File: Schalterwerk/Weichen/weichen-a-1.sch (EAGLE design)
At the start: 44 parts, among them J1 PHNX_2P_508CONN_1017491, Q1 P-MOSFET, Q2 P-MOSFET, Q3 P-MOSFET, Q4 P-MOSFET, X1 PHNX_4P_508CONN_1017493, X2 PHNX_4P_350CONN_1984989_PXC, X3 PHNX_4P_350CONN_1984989_PXC, X4 RJ45-JACK

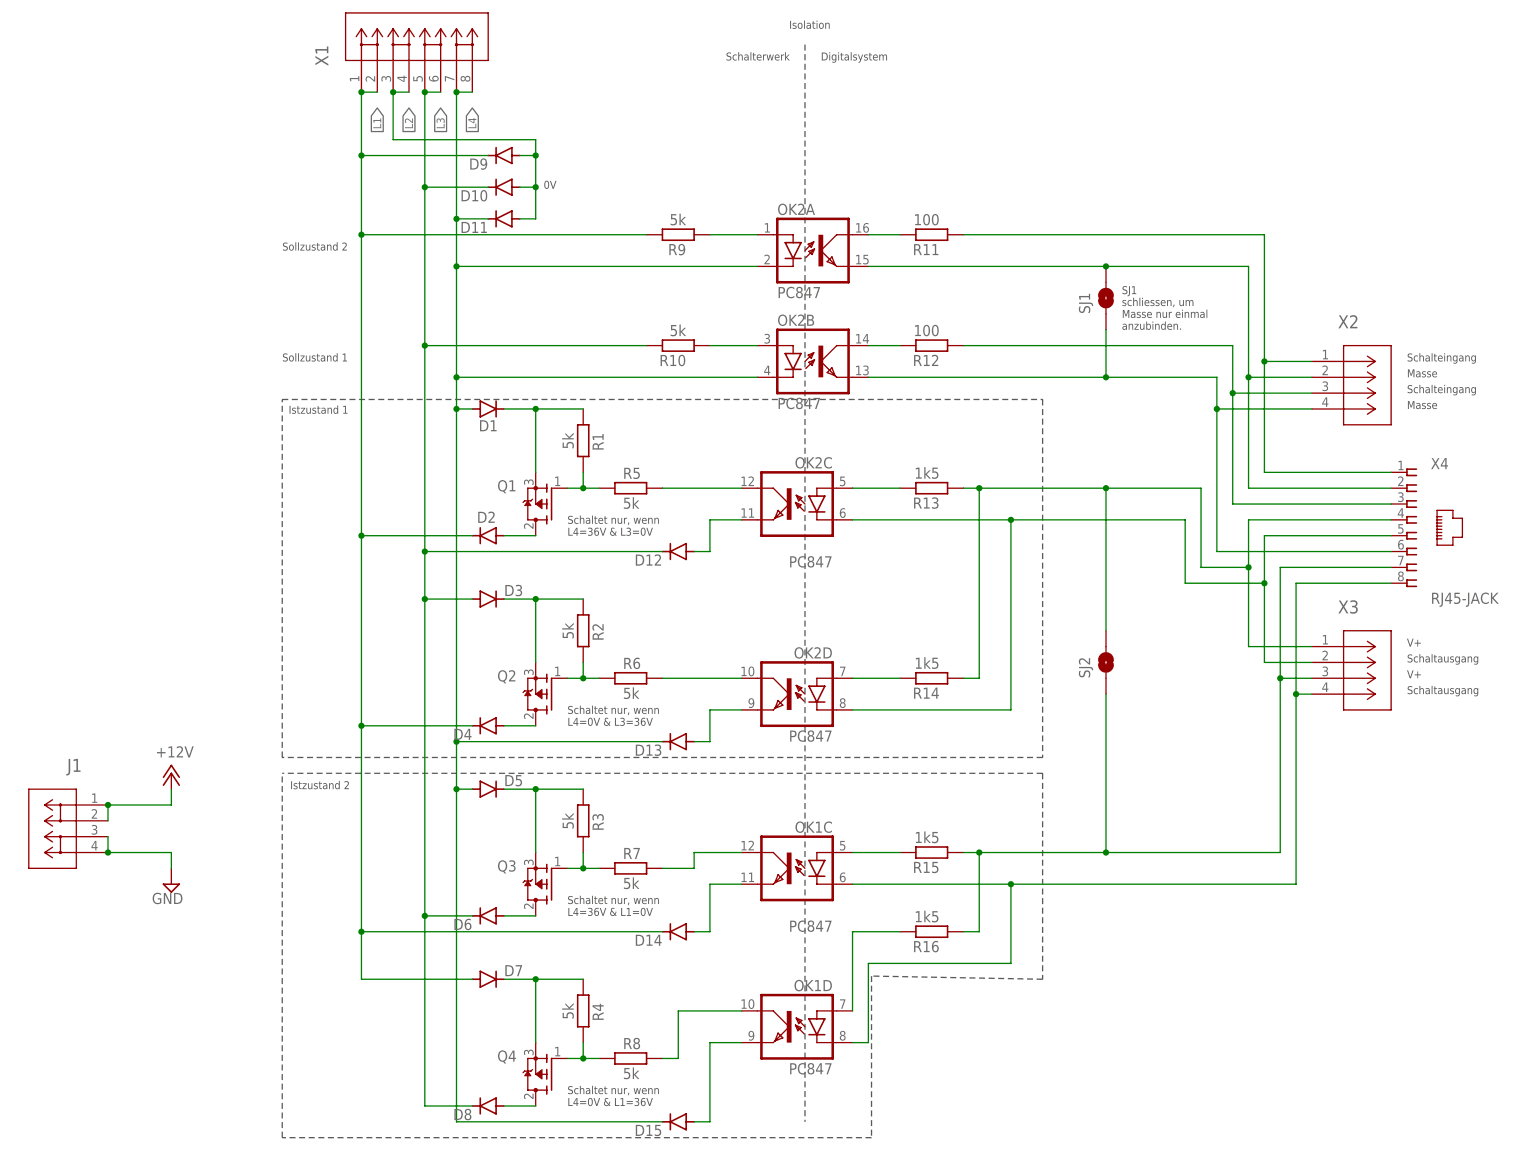
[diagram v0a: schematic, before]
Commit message: Updates the frames on the schematics with proper project information.
Adds LEDs for observing what is happening on the Gleisbelegtmeldung.
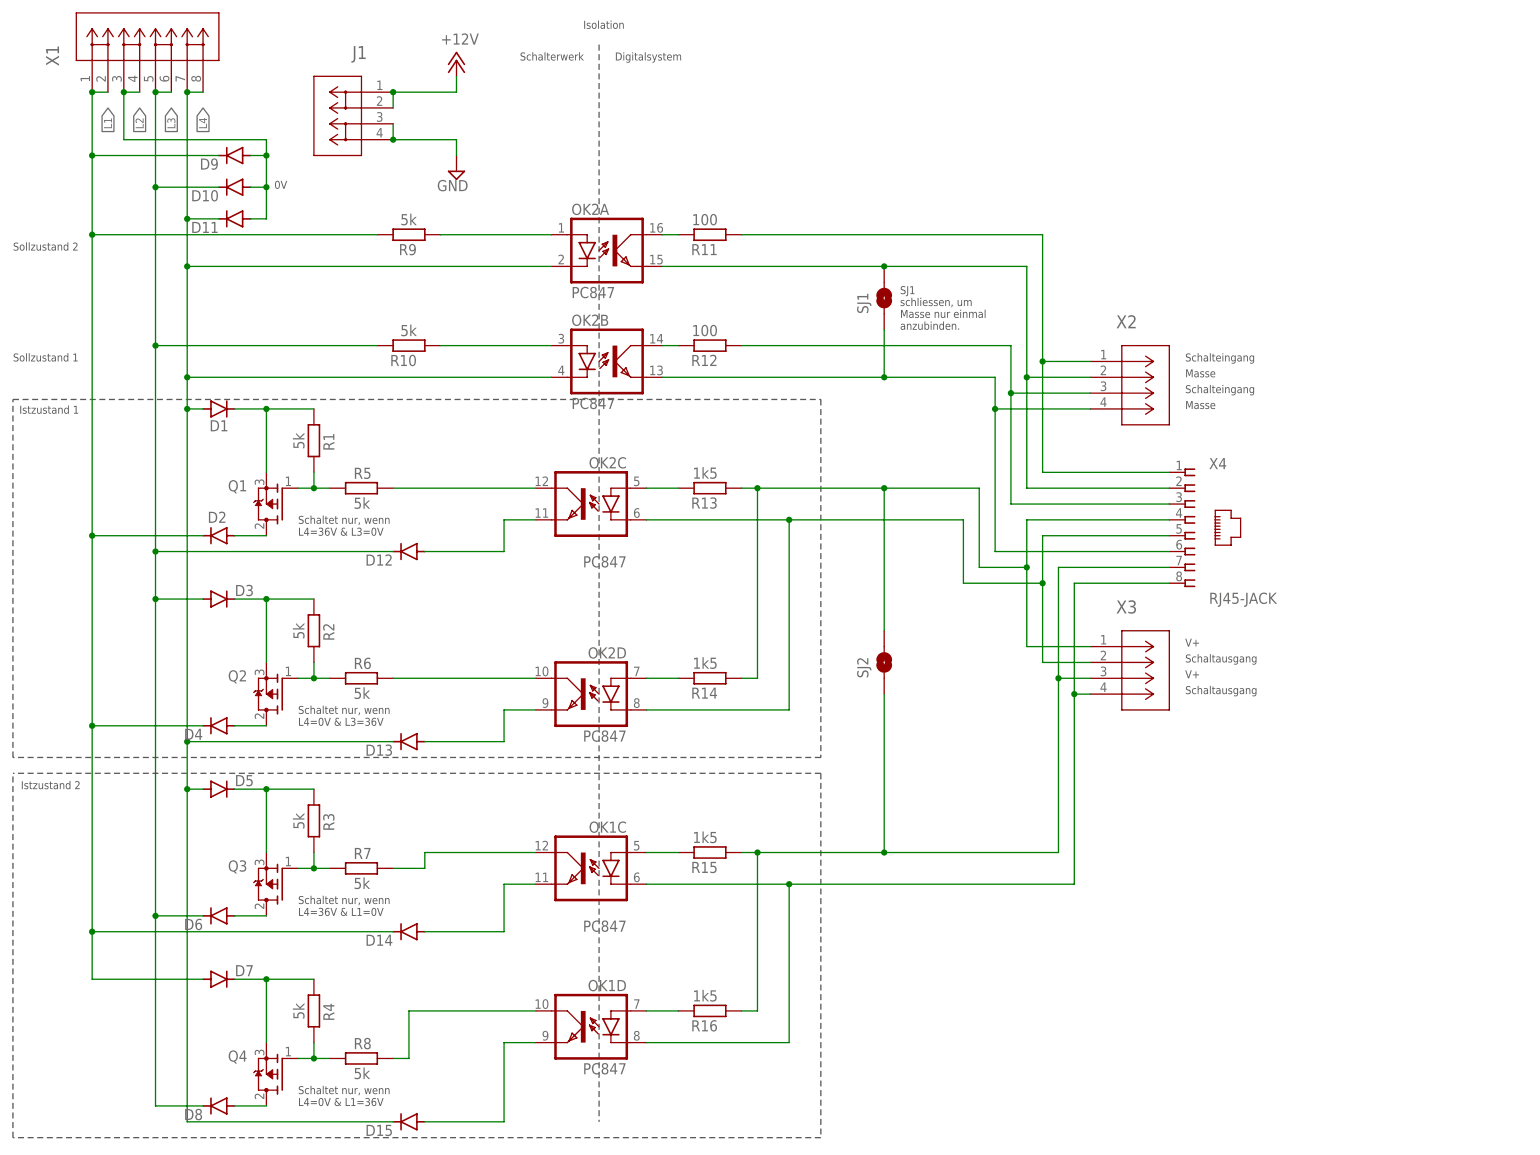
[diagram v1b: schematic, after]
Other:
- moved on the sheet: D1, D10, D11, D12, D13, D14, D15, D2, D3, D4, D5, D6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

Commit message: Closes out first release of Weichenschaltung.
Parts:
- added SJ3: (no value), eagleparts:SJRND2
- R1, R2, R3, R4: value 5k -> 10k
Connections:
- net GND: now also SJ3.1
- net L2: now also D10.C, D12.C, D3.A, D6.C, D8.C, R10.2, X1.5, X1.6; no longer D10.A, D11.A, D9.A, X1.3, X1.4
- net L3: now also D10.A, D11.A, D9.A, SJ3.2, X1.3, X1.4; no longer D10.C, D12.C, D3.A, D6.C, D8.C, R10.2, X1.5, X1.6
- net N$16: now also OK1A.C, OK1B.C; no longer OK1C.C, OK1D.C
- net N$24: now also OK1A.A; no longer OK1C.A
- net N$25: now also OK1B.A; no longer OK1D.A
- net N$27: now also OK1A.COL; no longer OK1C.COL
- net N$30: now also OK1B.COL; no longer OK1D.COL
- net N$35: now also OK1A.EMIT; no longer OK1C.EMIT
- net N$37: now also OK1B.EMIT; no longer OK1D.EMIT
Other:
- note added: "Rückmeldereingang"
- note removed: "Schalteingang"
- moved on the sheet: OK1C, OK1D
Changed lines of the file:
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@@
 <part name="D11" library="diode" library_urn="urn:adsk.eagle:library:210" deviceset="DIODE-" device="DO214AC" package3d_urn="urn:adsk.eagle:package:43417/2"/>
 <part name="Q1" library="eagleparts" deviceset="P-MOSFET" device=""/>
-<part name="R1" library="rcl" library_urn="urn:adsk.eagle:library:334" deviceset="R-EU_" device="R0805" package3d_urn="urn:adsk.eagle:package:23553/2" value="5k"/>
+<part name="R1" library="rcl" library_urn="urn:adsk.eagle:library:334" deviceset="R-EU_" device="R0805" package3d_urn="urn:adsk.eagle:package:23553/2" value="10k"/>
 <part name="R5" library="rcl" library_urn="urn:adsk.eagle:library:334" deviceset="R-EU_" device="R0805" package3d_urn="urn:adsk.eagle:package:23553/2" value="5k"/>
 <part name="Q2" library="eagleparts" deviceset="P-MOSFET" device=""/>
-<part name="R2" library="rcl" library_urn="urn:adsk.eagle:library:334" deviceset="R-EU_" device="R0805" package3d_urn="urn:adsk.eagle:package:23553/2" value="5k"/>
+<part name="R2" library="rcl" library_urn="urn:adsk.eagle:library:334" deviceset="R-EU_" device="R0805" package3d_urn="urn:adsk.eagle:package:23553/2" value="10k"/>
 <part name="R6" library="rcl" library_urn="urn:adsk.eagle:library:334" deviceset="R-EU_" device="R0805" package3d_urn="urn:adsk.eagle:package:23553/2" value="5k"/>
 <part name="J1" library="eagleparts" deviceset="PHNX_2P_508" device="CONN_1017491"/>
@@
 <part name="R16" library="rcl" library_urn="urn:adsk.eagle:library:334" deviceset="R-EU_" device="R0805" package3d_urn="urn:adsk.eagle:package:23553/2" value="1k5"/>
 <part name="Q3" library="eagleparts" deviceset="P-MOSFET" device=""/>
-<part name="R3" library="rcl" library_urn="urn:adsk.eagle:library:334" deviceset="R-EU_" device="R0805" package3d_urn="urn:adsk.eagle:package:23553/2" value="5k"/>
+<part name="R3" library="rcl" library_urn="urn:adsk.eagle:library:334" deviceset="R-EU_" device="R0805" package3d_urn="urn:adsk.eagle:package:23553/2" value="10k"/>
 <part name="R7" library="rcl" library_urn="urn:adsk.eagle:library:334" deviceset="R-EU_" device="R0805" package3d_urn="urn:adsk.eagle:package:23553/2" value="5k"/>
 <part name="Q4" library="eagleparts" deviceset="P-MOSFET" device=""/>
-<part name="R4" library="rcl" library_urn="urn:adsk.eagle:library:334" deviceset="R-EU_" device="R0805" package3d_urn="urn:adsk.eagle:package:23553/2" value="5k"/>
+<part name="R4" library="rcl" library_urn="urn:adsk.eagle:library:334" deviceset="R-EU_" device="R0805" package3d_urn="urn:adsk.eagle:package:23553/2" value="10k"/>
 <part name="R8" library="rcl" library_urn="urn:adsk.eagle:library:334" deviceset="R-EU_" device="R0805" package3d_urn="urn:adsk.eagle:package:23553/2" value="5k"/>
 <part name="D5" library="diode" library_urn="urn:adsk.eagle:library:210" deviceset="DIODE-" device="DO214AC" package3d_urn="urn:adsk.eagle:package:43417/2"/>
@@
 <part name="D8" library="diode" library_urn="urn:adsk.eagle:library:210" deviceset="DIODE-" device="DO214AC" package3d_urn="urn:adsk.eagle:package:43417/2"/>
 <part name="D7" library="diode" library_urn="urn:adsk.eagle:library:210" deviceset="DIODE-" device="DO214AC" package3d_urn="urn:adsk.eagle:package:43417/2"/>
+<part name="SJ3" library="eagleparts" deviceset="SJ" device="RND2"/>
 </parts>
 <sheets>
 <sheet>
 <plain>
-<text x="198.12" y="129.54" size="1.27" layer="97">Schalteingang</text>
-<text x="198.12" y="124.46" size="1.27" layer="97">Schalteingang</text>
+<text x="198.12" y="129.54" size="1.27" layer="97">Rückmeldereingang</text>
+<text x="198.12" y="124.46" size="1.27" layer="97">Rückmeldereingang</text>
 <text x="198.12" y="83.82" size="1.27" layer="97">V+</text>
 <text x="198.12" y="127" size="1.27" layer="97">Masse</text>
@@
 <attribute name="VALUE" x="123.19" y="82.042" size="1.778" layer="96" rot="R180"/>
 </instance>
-<instance part="OK1" gate="C" x="101.6" y="48.26" smashed="yes" rot="MR0">
+<instance part="OK1" gate="A" x="101.6" y="48.26" smashed="yes" rot="MR0">
 <attribute name="NAME" x="108.585" y="53.975" size="1.778" layer="95" rot="MR0"/>
 <attribute name="VALUE" x="108.585" y="38.1" size="1.778" layer="96" rot="MR0"/>
 </instance>
-<instance part="OK1" gate="D" x="101.6" y="22.86" smashed="yes" rot="MR0">
+<instance part="OK1" gate="B" x="101.6" y="22.86" smashed="yes" rot="MR0">
 <attribute name="NAME" x="108.585" y="28.575" size="1.778" layer="95" rot="MR0"/>
 <attribute name="VALUE" x="108.585" y="15.24" size="1.778" layer="96" rot="MR0"/>
@@
 <attribute name="NAME" x="45.72" y="30.9626" size="1.778" layer="95"/>
 <attribute name="VALUE" x="45.72" y="28.1686" size="1.778" layer="96"/>
+</instance>
+<instance part="SJ3" gate="1" x="63.5" y="154.94" smashed="yes" rot="R180">
+<attribute name="NAME" x="66.04" y="152.4" size="1.778" layer="95" rot="R180"/>
+<attribute name="VALUE" x="66.04" y="158.75" size="1.778" layer="96" rot="R180"/>
+</instance>
+<instance part="OK1" gate="D" x="203.2" y="53.34" smashed="yes">
+<attribute name="NAME" x="196.215" y="59.055" size="1.778" layer="95"/>
+<attribute name="VALUE" x="196.215" y="45.72" size="1.778" layer="96"/>
+</instance>
+<instance part="OK1" gate="C" x="223.52" y="43.18" smashed="yes">
+<attribute name="NAME" x="216.535" y="48.895" size="1.778" layer="95"/>
+<attribute name="VALUE" x="216.535" y="35.56" size="1.778" layer="96"/>
 </instance>
 </instances>
@@
 <wire x1="180.34" y1="76.2" x2="182.88" y2="76.2" width="0.1524" layer="91"/>
 <junction x="180.34" y="76.2"/>
-<pinref part="OK1" gate="C" pin="C"/>
+<pinref part="OK1" gate="A" pin="C"/>
 <wire x1="111.76" y1="45.72" x2="134.62" y2="45.72" width="0.1524" layer="91"/>
-<pinref part="OK1" gate="D" pin="C"/>
+<pinref part="OK1" gate="B" pin="C"/>
 <wire x1="134.62" y1="45.72" x2="180.34" y2="45.72" width="0.1524" layer="91"/>
 <wire x1="111.76" y1="20.32" x2="134.62" y2="20.32" width="0.1524" layer="91"/>
@@
 <wire x1="71.12" y1="167.64" x2="71.12" y2="165.1" width="0.1524" layer="91"/>
 <pinref part="SUPPLY4" gate="GND" pin="GND"/>
-<wire x1="71.12" y1="165.1" x2="81.28" y2="165.1" width="0.1524" layer="91"/>
+<wire x1="71.12" y1="165.1" x2="73.66" y2="165.1" width="0.1524" layer="91"/>
+<wire x1="73.66" y1="165.1" x2="81.28" y2="165.1" width="0.1524" layer="91"/>
 <wire x1="81.28" y1="165.1" x2="81.28" y2="162.56" width="0.1524" layer="91"/>
 <junction x="71.12" y="165.1"/>
+<pinref part="SJ3" gate="1" pin="1"/>
+<wire x1="68.58" y1="154.94" x2="73.66" y2="154.94" width="0.1524" layer="91"/>
+<wire x1="73.66" y1="154.94" x2="73.66" y2="165.1" width="0.1524" layer="91"/>
+<junction x="73.66" y="165.1"/>
 </segment>
 </net>
@@
 </segment>
 </net>
-<net name="L2" class="0">
+<net name="L3" class="0">
 <segment>
 <pinref part="X1" gate="A" pin="3"/>
@@
 <pinref part="D11" gate="G$1" pin="A"/>
 <wire x1="48.26" y1="152.4" x2="50.8" y2="152.4" width="0.1524" layer="91"/>
-<wire x1="50.8" y1="152.4" x2="50.8" y2="157.48" width="0.1524" layer="91"/>
+<wire x1="50.8" y1="152.4" x2="50.8" y2="154.94" width="0.1524" layer="91"/>
 <pinref part="D9" gate="G$1" pin="A"/>
+<wire x1="50.8" y1="154.94" x2="50.8" y2="157.48" width="0.1524" layer="91"/>
 <wire x1="50.8" y1="157.48" x2="50.8" y2="162.56" width="0.1524" layer="91"/>
 <wire x1="50.8" y1="162.56" x2="48.26" y2="162.56" width="0.1524" layer="91"/>
@@
 <wire x1="27.94" y1="165.1" x2="27.94" y2="172.72" width="0.1524" layer="91"/>
 <junction x="27.94" y="172.72"/>
+<pinref part="SJ3" gate="1" pin="2"/>
+<wire x1="50.8" y1="154.94" x2="58.42" y2="154.94" width="0.1524" layer="91"/>
+<junction x="50.8" y="154.94"/>
 </segment>
 </net>
@@
 <segment>
 <pinref part="R15" gate="G$1" pin="2"/>
-<pinref part="OK1" gate="C" pin="A"/>
+<pinref part="OK1" gate="A" pin="A"/>
 <wire x1="116.84" y1="50.8" x2="111.76" y2="50.8" width="0.1524" layer="91"/>
 </segment>
@@
 <net name="N$25" class="0">
 <segment>
-<pinref part="OK1" gate="D" pin="A"/>
+<pinref part="OK1" gate="B" pin="A"/>
 <pinref part="R16" gate="G$1" pin="2"/>
 <wire x1="111.76" y1="25.4" x2="116.84" y2="25.4" width="0.1524" layer="91"/>
@@
 <wire x1="88.9" y1="45.72" x2="88.9" y2="38.1" width="0.1524" layer="91"/>
 <wire x1="88.9" y1="38.1" x2="76.2" y2="38.1" width="0.1524" layer="91"/>
-<pinref part="OK1" gate="C" pin="EMIT"/>
+<pinref part="OK1" gate="A" pin="EMIT"/>
 </segment>
 </net>
@@
 <pinref part="D15" gate="G$1" pin="A"/>
 <wire x1="88.9" y1="7.62" x2="76.2" y2="7.62" width="0.1524" layer="91"/>
-<pinref part="OK1" gate="D" pin="EMIT"/>
+<pinref part="OK1" gate="B" pin="EMIT"/>
 <wire x1="93.98" y1="20.32" x2="88.9" y2="20.32" width="0.1524" layer="91"/>
 <wire x1="88.9" y1="20.32" x2="88.9" y2="7.62" width="0.1524" layer="91"/>
@@
 <net name="N$27" class="0">
 <segment>
-<pinref part="OK1" gate="C" pin="COL"/>
+<pinref part="OK1" gate="A" pin="COL"/>
 <wire x1="93.98" y1="50.8" x2="76.2" y2="50.8" width="0.1524" layer="91"/>
 <wire x1="76.2" y1="50.8" x2="76.2" y2="48.26" width="0.1524" layer="91"/>
@@
 <wire x1="71.12" y1="17.78" x2="73.66" y2="17.78" width="0.1524" layer="91"/>
 <wire x1="73.66" y1="17.78" x2="73.66" y2="25.4" width="0.1524" layer="91"/>
-<pinref part="OK1" gate="D" pin="COL"/>
+<pinref part="OK1" gate="B" pin="COL"/>
 <wire x1="73.66" y1="25.4" x2="93.98" y2="25.4" width="0.1524" layer="91"/>
 </segment>
@@
 </segment>
 </net>
-<net name="L3" class="0">
+<net name="L2" class="0">
 <segment>
 <pinref part="D6" gate="G$1" pin="C"/>
